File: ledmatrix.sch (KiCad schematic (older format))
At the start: 75 parts, among them SW1 SPST

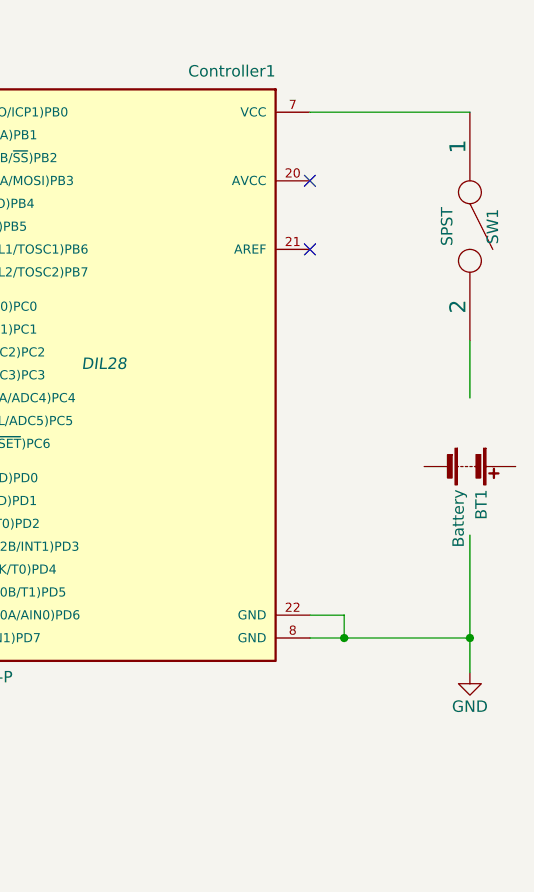
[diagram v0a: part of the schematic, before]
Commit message: fixed power flag problem, now it runs ERC
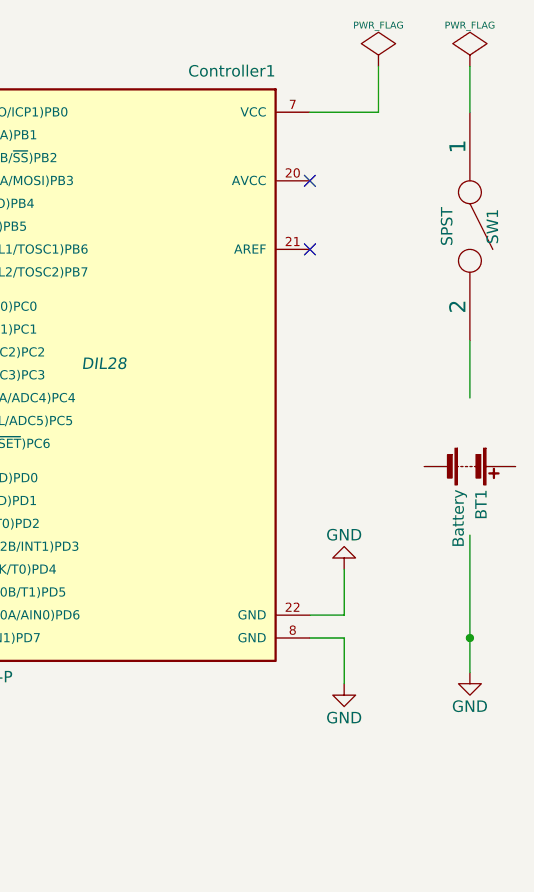
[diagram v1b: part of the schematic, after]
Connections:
- wire segments 102 -> 105
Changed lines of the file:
@@
 Sheet 1 1
 Title "Atmel led matrix"
-Date "11 jun 2016"
+Date "14 sep 2016"
 Rev "1"
 Comp "Nangoniac"
@@
 Wire Wire Line
 	1600 6950 3900 6950
-Wire Wire Line
-	8150 3250 8850 3250
-Wire Wire Line
-	8150 3150 8300 3150
-Wire Wire Line
-	8300 3150 8300 3250
-Connection ~ 8300 3250
 $Comp
 L Battery BT1
@@
 	0    1    1    0
 $EndComp
-Wire Wire Line
-	8150 950  8850 950
 Wire Wire Line
 	8850 2800 8850 3400
@@
 Connection ~ 2300 2500
 Connection ~ 8850 3250
+$Comp
+L PWR_FLAG #FLG02
+U 1 1 57D941F4
+P 8450 750
+F 0 "#FLG02" H 8450 845 30  0001 C CNN
+F 1 "PWR_FLAG" H 8450 930 30  0000 C CNN
+F 2 "" H 8450 750 60  0000 C CNN
+F 3 "" H 8450 750 60  0000 C CNN
+	1    8450 750
+	1    0    0    -1
+$EndComp
+$Comp
+L PWR_FLAG #FLG03
+U 1 1 57D942AF
+P 8850 750
+F 0 "#FLG03" H 8850 845 30  0001 C CNN
+F 1 "PWR_FLAG" H 8850 930 30  0000 C CNN
+F 2 "" H 8850 750 60  0000 C CNN
+F 3 "" H 8850 750 60  0000 C CNN
+	1    8850 750
+	1    0    0    -1
+$EndComp
+Wire Wire Line
+	8850 750  8850 950
+$Comp
+L GND #PWR?
+U 1 1 57D94359
+P 8300 3450
+F 0 "#PWR?" H 8300 3200 50  0001 C CNN
+F 1 "GND" H 8300 3300 50  0000 C CNN
+F 2 "" H 8300 3450 50  0000 C CNN
+F 3 "" H 8300 3450 50  0000 C CNN
+	1    8300 3450
+	1    0    0    -1
+$EndComp
+$Comp
+L GND #PWR?
+U 1 1 57D9435F
+P 8300 2950
+F 0 "#PWR?" H 8300 2700 50  0001 C CNN
+F 1 "GND" H 8300 2800 50  0000 C CNN
+F 2 "" H 8300 2950 50  0000 C CNN
+F 3 "" H 8300 2950 50  0000 C CNN
+	1    8300 2950
+	-1   0    0    1
+$EndComp
+Wire Wire Line
+	8150 3150 8300 3150
+Wire Wire Line
+	8300 3150 8300 2950
+Wire Wire Line
+	8150 3250 8300 3250
+Wire Wire Line
+	8300 3250 8300 3450
+Wire Wire Line
+	8150 950  8450 950
+Wire Wire Line
+	8450 950  8450 750
 $EndSCHEMATC

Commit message: Update
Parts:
- Controller1: symbol ATMEGA328-P -> ATMEGA328-P-RESCUE-ledmatrix
- D1, D10, D11, D12, D13, D14, D15, D16, D17, D18, D19, D2, D20, D21, D22, D23, D24, D25, D26, D27, D28, D29, D3, D30, D31, D32, D33, D34, D35, D36, D37, D38, D39, D4, D40, D41, D42, D43, D44, D45, D46, D47, D48, D49, D5, D50, D51, D52, D53, D54, D55, D56, D57, D58, D59, D6, D60, D61, D62, D63, D64, D7, D8, D9: symbol LED -> LED-RESCUE-ledmatrix
- R1, R2, R3, R4, R5, R6, R7, R8: symbol R -> R-RESCUE-ledmatrix
